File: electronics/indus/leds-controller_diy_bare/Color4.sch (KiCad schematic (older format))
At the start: 19 parts, among them Q5 Q_NPN_BCE, U3 TPS92513

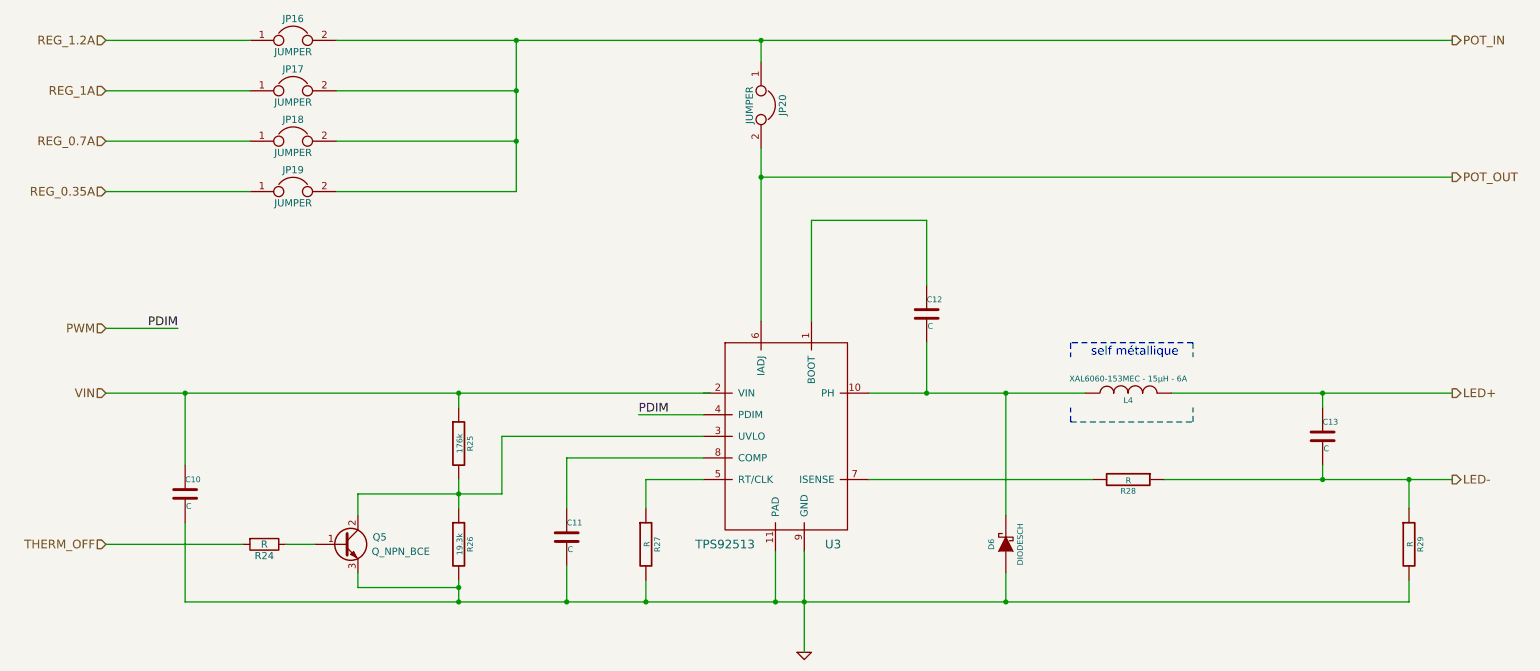
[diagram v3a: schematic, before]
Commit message: Added missing Capa & Resistor values
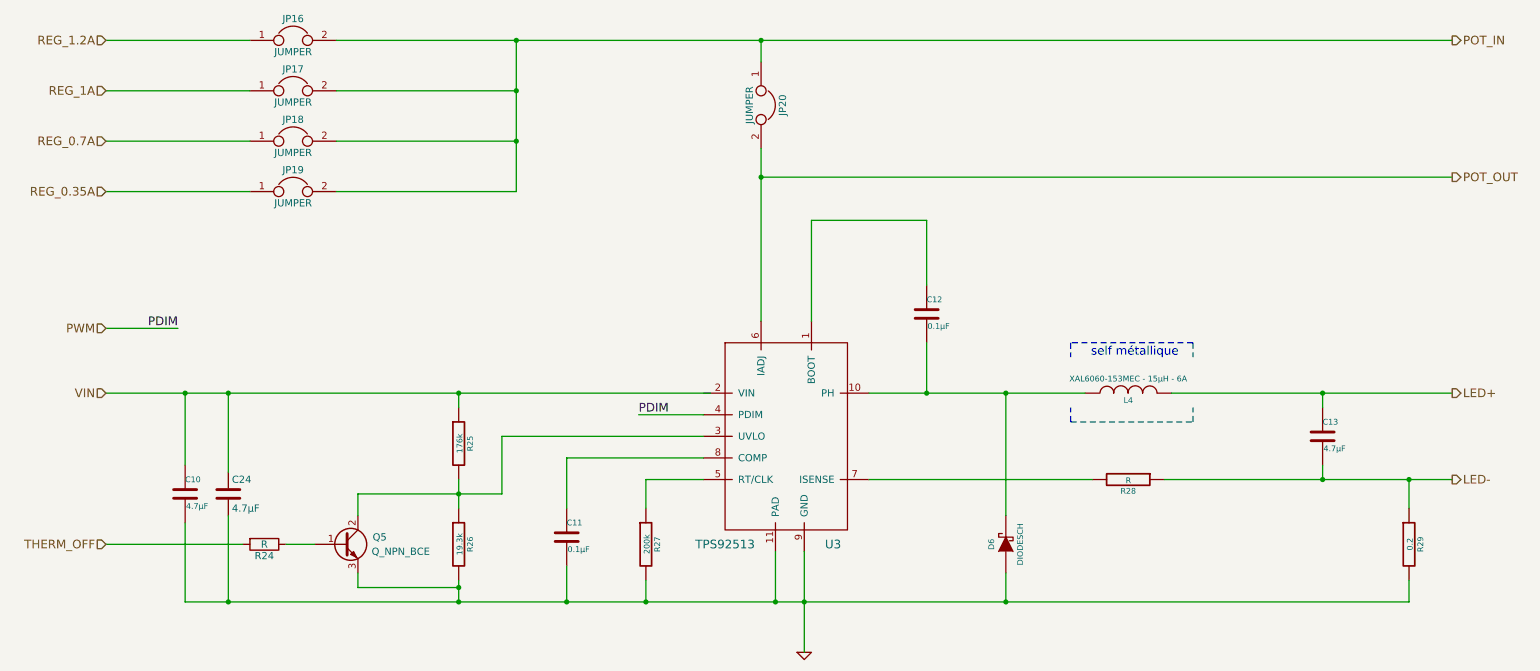
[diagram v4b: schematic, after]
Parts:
- added C24: 4.7µF, symbol C
- C10, C13: value C -> 4.7µF
- C11, C12: value C -> 0.1µF
- R27: value R -> 200k
- R29: value R -> 0.2
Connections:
- net GND: now also C24.2
- net VIN: now also C24.1
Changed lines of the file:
@@
 P 1800 4700
 F 0 "C10" H 1800 4800 40  0000 L CNN
-F 1 "C" H 1806 4615 40  0000 L CNN
+F 1 "4.7µF" H 1806 4615 40  0000 L CNN
 F 2 "" H 1838 4550 30  0000 C CNN
 F 3 "" H 1800 4700 60  0000 C CNN
@@
 P 4450 5000
 F 0 "C11" H 4450 5100 40  0000 L CNN
-F 1 "C" H 4456 4915 40  0000 L CNN
+F 1 "0.1µF" H 4456 4915 40  0000 L CNN
 F 2 "" H 4488 4850 30  0000 C CNN
 F 3 "" H 4450 5000 60  0000 C CNN
@@
 P 5000 5050
 F 0 "R27" V 5080 5050 40  0000 C CNN
-F 1 "R" V 5007 5051 40  0000 C CNN
+F 1 "200k" V 5007 5051 40  0000 C CNN
 F 2 "" V 4930 5050 30  0000 C CNN
 F 3 "" H 5000 5050 30  0000 C CNN
@@
 P 6950 3450
 F 0 "C12" H 6950 3550 40  0000 L CNN
-F 1 "C" H 6956 3365 40  0000 L CNN
+F 1 "0.1µF" H 6956 3365 40  0000 L CNN
 F 2 "" H 6988 3300 30  0000 C CNN
 F 3 "" H 6950 3450 60  0000 C CNN
@@
 P 9700 4300
 F 0 "C13" H 9700 4400 40  0000 L CNN
-F 1 "C" H 9706 4215 40  0000 L CNN
+F 1 "4.7µF" H 9706 4215 40  0000 L CNN
 F 2 "" H 9738 4150 30  0000 C CNN
 F 3 "" H 9700 4300 60  0000 C CNN
@@
 P 10300 5050
 F 0 "R29" V 10380 5050 40  0000 C CNN
-F 1 "R" V 10307 5051 40  0000 C CNN
+F 1 "0.2" V 10307 5051 40  0000 C CNN
 F 2 "" V 10230 5050 30  0000 C CNN
 F 3 "" H 10300 5050 30  0000 C CNN
@@
 POT_OUT
 Wire Wire Line
-	1250 4000 1800 4000
-Wire Wire Line
-	1800 4000 3700 4000
-Wire Wire Line
-	3700 4000 3700 4000
-Wire Wire Line
-	3700 4000 5450 4000
-Wire Wire Line
-	1800 5450 3700 5450
-Wire Wire Line
-	3700 5450 4450 5450
-Wire Wire Line
-	4450 5450 5000 5450
-Wire Wire Line
-	5000 5450 5900 5450
-Wire Wire Line
-	5900 5450 6100 5450
-Wire Wire Line
-	6100 5450 7500 5450
-Wire Wire Line
-	7500 5450 10300 5450
-Wire Wire Line
-	6100 5100 6100 5450
-Wire Wire Line
-	6100 5450 6100 5800
+	1250 4000 5450 4000
+Wire Wire Line
+	1800 5450 10300 5450
+Wire Wire Line
+	6100 5100 6100 5800
 Wire Wire Line
 	5900 5100 5900 5450
@@
 Connection ~ 6100 5450
 Wire Wire Line
-	3700 4600 3700 4700
-Wire Wire Line
-	3700 4700 3700 4800
+	3700 4600 3700 4800
 Wire Wire Line
 	4000 4700 4000 4300
@@
 	8800 3650 8800 3750
 Wire Wire Line
-	6550 4000 6950 4000
-Wire Wire Line
-	6950 4000 7500 4000
-Wire Wire Line
-	7500 4000 8050 4000
+	6550 4000 8050 4000
 Wire Wire Line
 	6150 3500 6150 2800
@@
 Connection ~ 6950 4000
 Wire Wire Line
-	8650 4000 9700 4000
-Wire Wire Line
-	9700 4000 10600 4000
+	8650 4000 10600 4000
 Wire Wire Line
 	9700 4100 9700 4000
@@
 	6550 4600 8100 4600
 Wire Wire Line
-	8600 4600 9700 4600
-Wire Wire Line
-	9700 4600 10300 4600
-Wire Wire Line
-	10300 4600 10600 4600
+	8600 4600 10600 4600
 Wire Wire Line
 	10300 4800 10300 4600
@@
 	1250 2600 2250 2600
 Wire Wire Line
-	2850 1550 4100 1550
-Wire Wire Line
-	4100 1550 5800 1550
-Wire Wire Line
-	5800 1550 10600 1550
+	2850 1550 10600 1550
 Wire Wire Line
 	2850 1900 4100 1900
 Wire Wire Line
-	4100 1550 4100 1900
-Wire Wire Line
-	4100 1900 4100 2250
-Wire Wire Line
-	4100 2250 4100 2600
+	4100 1550 4100 2600
 Connection ~ 4100 1550
 Wire Wire Line
@@
 Connection ~ 5800 2500
 Wire Wire Line
-	5800 2300 5800 2500
-Wire Wire Line
-	5800 2500 5800 3500
+	5800 2300 5800 3500
 Wire Wire Line
 	5800 1700 5800 1550
@@
 	1800 4900 1800 5450
 Wire Wire Line
-	3700 5300 3700 5350
-Wire Wire Line
-	3700 5350 3700 5450
+	3700 5300 3700 5450
 Wire Wire Line
 	3700 4100 3700 4000
@@
 	3000 4850 3000 4700
 Wire Wire Line
-	3000 4700 3700 4700
-Wire Wire Line
-	3700 4700 4000 4700
+	3000 4700 4000 4700
 Wire Wire Line
 	3000 5250 3000 5350
@@
 Wire Wire Line
 	2200 5050 1250 5050
+$Comp
+L C C24
+U 1 1 576AC01B
+P 2100 4700
+F 0 "C24" H 2125 4800 50  0000 L CNN
+F 1 "4.7µF" H 2125 4600 50  0000 L CNN
+F 2 "" H 2138 4550 50  0000 C CNN
+F 3 "" H 2100 4700 50  0000 C CNN
+	1    2100 4700
+	1    0    0    -1
+$EndComp
+Wire Wire Line
+	2100 4550 2100 4000
+Connection ~ 2100 4000
+Wire Wire Line
+	2100 4850 2100 5450
+Connection ~ 2100 5450
 $EndSCHEMATC

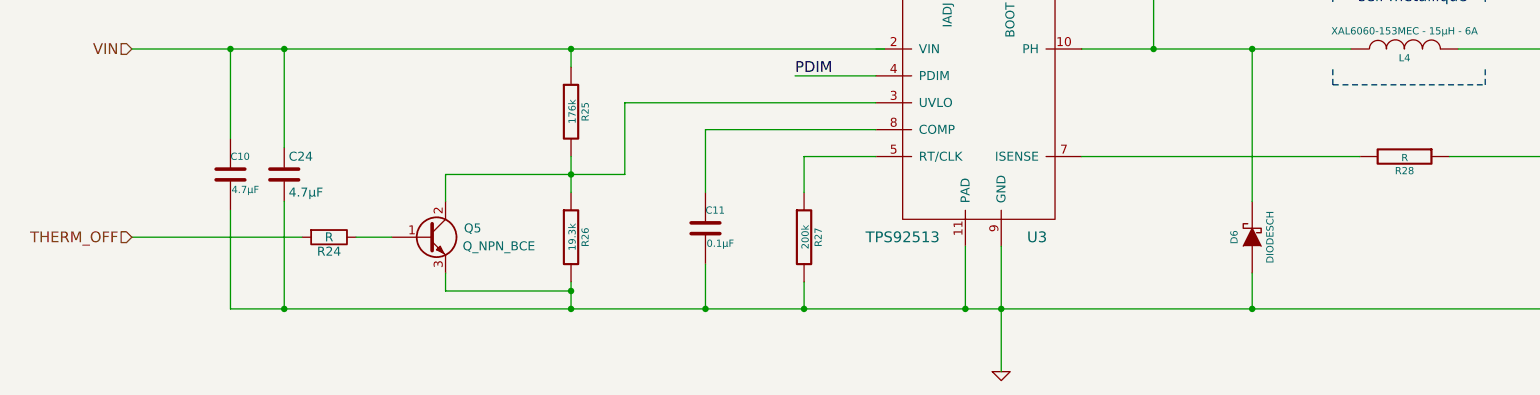
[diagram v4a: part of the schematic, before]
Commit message: footprint with libraries
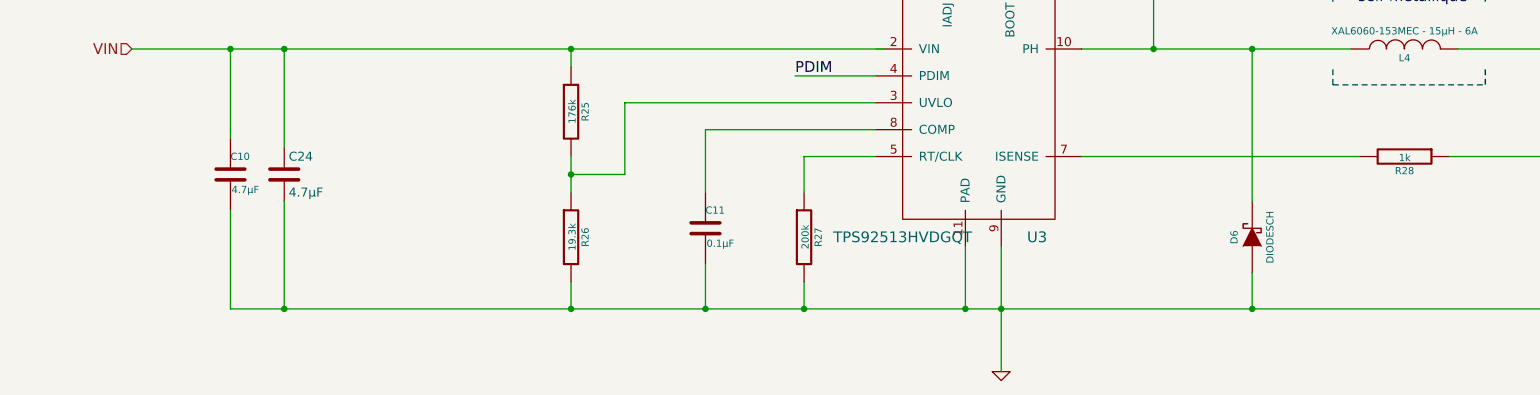
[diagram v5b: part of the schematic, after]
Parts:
- removed Q5: Q_NPN_BCE, symbol Q_NPN_BCE
- removed R24: R, symbol R
- C10, C13, C24: footprint (none) -> Capacitors_SMD:C_1206
- C11, C12: footprint (none) -> Capacitors_SMD:C_0805
- D6: footprint (none) -> Diodes_SMD:SOD-123
- R25, R26, R27: footprint (none) -> Resistors_SMD:R_0805
- R28: value R -> 1k; footprint (none) -> Resistors_SMD:R_0805
- R29: footprint (none) -> Resistors_SMD:R_1206
- U3: value TPS92513 -> TPS92513HVDGQT; footprint (none) -> risebox:BUCK_TPS92513_PowerPAD
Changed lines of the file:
@@
 P 5950 4100
 F 0 "U3" H 6300 3150 60  0000 C CNN
-F 1 "TPS92513" H 5550 3150 60  0000 C CNN
-F 2 "" H 6100 4200 60  0000 C CNN
+F 1 "TPS92513HVDGQT" H 5550 3150 60  0000 C CNN
+F 2 "risebox:BUCK_TPS92513_PowerPAD" H 6100 4200 60  0001 C CNN
 F 3 "" H 6100 4200 60  0000 C CNN
 	1    5950 4100
@@
 F 0 "C10" H 1800 4800 40  0000 L CNN
 F 1 "4.7µF" H 1806 4615 40  0000 L CNN
-F 2 "" H 1838 4550 30  0000 C CNN
+F 2 "Capacitors_SMD:C_1206" H 1838 4550 30  0001 C CNN
 F 3 "" H 1800 4700 60  0000 C CNN
 	1    1800 4700
@@
 $EndComp
 $Comp
-L GND-RESCUE-leds-controller #PWR14
+L GND-RESCUE-leds-controller #PWR015
 U 1 1 5767300B
 P 6100 5800
-F 0 "#PWR14" H 6100 5800 30  0001 C CNN
+F 0 "#PWR015" H 6100 5800 30  0001 C CNN
 F 1 "GND" H 6100 5730 30  0001 C CNN
 F 2 "" H 6100 5800 60  0000 C CNN
@@
 F 0 "R25" V 3780 4350 40  0000 C CNN
 F 1 "176k" V 3707 4351 40  0000 C CNN
-F 2 "" V 3630 4350 30  0000 C CNN
+F 2 "Resistors_SMD:R_0805" V 3630 4350 30  0001 C CNN
 F 3 "" H 3700 4350 30  0000 C CNN
 	1    3700 4350
@@
 F 0 "R26" V 3780 5050 40  0000 C CNN
 F 1 "19.3k" V 3707 5051 40  0000 C CNN
-F 2 "" V 3630 5050 30  0000 C CNN
+F 2 "Resistors_SMD:R_0805" V 3630 5050 30  0001 C CNN
 F 3 "" H 3700 5050 30  0000 C CNN
 	1    3700 5050
@@
 F 0 "C11" H 4450 5100 40  0000 L CNN
 F 1 "0.1µF" H 4456 4915 40  0000 L CNN
-F 2 "" H 4488 4850 30  0000 C CNN
+F 2 "Capacitors_SMD:C_0805" H 4488 4850 30  0001 C CNN
 F 3 "" H 4450 5000 60  0000 C CNN
 	1    4450 5000
@@
 F 0 "R27" V 5080 5050 40  0000 C CNN
 F 1 "200k" V 5007 5051 40  0000 C CNN
-F 2 "" V 4930 5050 30  0000 C CNN
+F 2 "Resistors_SMD:R_0805" V 4930 5050 30  0001 C CNN
 F 3 "" H 5000 5050 30  0000 C CNN
 	1    5000 5050
@@
 F 0 "C12" H 6950 3550 40  0000 L CNN
 F 1 "0.1µF" H 6956 3365 40  0000 L CNN
-F 2 "" H 6988 3300 30  0000 C CNN
+F 2 "Capacitors_SMD:C_0805" H 6988 3300 30  0001 C CNN
 F 3 "" H 6950 3450 60  0000 C CNN
 	1    6950 3450
@@
 F 0 "C13" H 9700 4400 40  0000 L CNN
 F 1 "4.7µF" H 9706 4215 40  0000 L CNN
-F 2 "" H 9738 4150 30  0000 C CNN
+F 2 "Capacitors_SMD:C_1206" H 9738 4150 30  0001 C CNN
 F 3 "" H 9700 4300 60  0000 C CNN
 	1    9700 4300
@@
 P 8350 4600
 F 0 "R28" V 8430 4600 40  0000 C CNN
-F 1 "R" V 8357 4601 40  0000 C CNN
-F 2 "" V 8280 4600 30  0000 C CNN
+F 1 "1k" V 8357 4601 40  0000 C CNN
+F 2 "Resistors_SMD:R_0805" V 8280 4600 30  0001 C CNN
 F 3 "" H 8350 4600 30  0000 C CNN
 	1    8350 4600
@@
 F 0 "R29" V 10380 5050 40  0000 C CNN
 F 1 "0.2" V 10307 5051 40  0000 C CNN
-F 2 "" V 10230 5050 30  0000 C CNN
+F 2 "Resistors_SMD:R_1206" V 10230 5050 30  0001 C CNN
 F 3 "" H 10300 5050 30  0000 C CNN
 	1    10300 5050
@@
 F 0 "D6" H 7500 5150 40  0000 C CNN
 F 1 "DIODESCH" H 7500 4950 40  0000 C CNN
-F 2 "" H 7500 5050 60  0000 C CNN
+F 2 "Diodes_SMD:SOD-123" H 7500 5050 60  0001 C CNN
 F 3 "" H 7500 5050 60  0000 C CNN
 	1    7500 5050
@@
 F 0 "JP16" H 2550 1700 50  0000 C CNN
 F 1 "JUMPER" H 2550 1470 50  0000 C CNN
-F 2 "" H 2550 1550 50  0000 C CNN
+F 2 "" H 2550 1550 50  0001 C CNN
 F 3 "" H 2550 1550 50  0000 C CNN
 	1    2550 1550
@@
 F 0 "JP17" H 2550 2050 50  0000 C CNN
 F 1 "JUMPER" H 2550 1820 50  0000 C CNN
-F 2 "" H 2550 1900 50  0000 C CNN
+F 2 "" H 2550 1900 50  0001 C CNN
 F 3 "" H 2550 1900 50  0000 C CNN
 	1    2550 1900
@@
 F 0 "JP18" H 2550 2400 50  0000 C CNN
 F 1 "JUMPER" H 2550 2170 50  0000 C CNN
-F 2 "" H 2550 2250 50  0000 C CNN
+F 2 "" H 2550 2250 50  0001 C CNN
 F 3 "" H 2550 2250 50  0000 C CNN
 	1    2550 2250
@@
 F 0 "JP19" H 2550 2750 50  0000 C CNN
 F 1 "JUMPER" H 2550 2520 50  0000 C CNN
-F 2 "" H 2550 2600 50  0000 C CNN
+F 2 "" H 2550 2600 50  0001 C CNN
 F 3 "" H 2550 2600 50  0000 C CNN
 	1    2550 2600
@@
 F 0 "JP20" H 5800 2150 50  0000 C CNN
 F 1 "JUMPER" H 5800 1920 50  0000 C CNN
-F 2 "" H 5800 2000 50  0000 C CNN
+F 2 "" H 5800 2000 50  0001 C CNN
 F 3 "" H 5800 2000 50  0000 C CNN
 	1    5800 2000
@@
 Connection ~ 3700 5450
 Wire Wire Line
-	3000 4850 3000 4700
-Wire Wire Line
-	3000 4700 4000 4700
-Wire Wire Line
-	3000 5250 3000 5350
-Wire Wire Line
-	3000 5350 3700 5350
-Connection ~ 3700 5350
-$Comp
-L Q_NPN_BCE Q5
-U 1 1 576730E6
-P 2900 5050
-F 0 "Q5" H 3200 5100 50  0000 R CNN
-F 1 "Q_NPN_BCE" H 3500 5000 50  0000 R CNN
-F 2 "" H 3100 5150 50  0000 C CNN
-F 3 "" H 2900 5050 50  0000 C CNN
-	1    2900 5050
-	1    0    0    -1
-$EndComp
-Text HLabel 1250 5050 0    60   Input ~ 0
-THERM_OFF
-$Comp
-L R R24
-U 1 1 576730EE
-P 2350 5050
-F 0 "R24" V 2430 5050 50  0000 C CNN
-F 1 "R" V 2350 5050 50  0000 C CNN
-F 2 "" V 2280 5050 50  0000 C CNN
-F 3 "" H 2350 5050 50  0000 C CNN
-	1    2350 5050
-	0    1    1    0
-$EndComp
-Wire Wire Line
-	2500 5050 2700 5050
-Wire Wire Line
-	2200 5050 1250 5050
+	3700 4700 4000 4700
 $Comp
 L C C24
@@
 F 0 "C24" H 2125 4800 50  0000 L CNN
 F 1 "4.7µF" H 2125 4600 50  0000 L CNN
-F 2 "" H 2138 4550 50  0000 C CNN
+F 2 "Capacitors_SMD:C_1206" H 2138 4550 50  0001 C CNN
 F 3 "" H 2100 4700 50  0000 C CNN
 	1    2100 4700

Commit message: fix some errors
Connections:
- net VIN: now also U3.2 (VIN)
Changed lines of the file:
@@
 Text HLabel 10600 4600 2    60   Output ~ 0
 LED-
-Text HLabel 1250 4000 0    60   Input ~ 0
+Text HLabel 1300 4000 0    60   Input ~ 0
 VIN
 $Comp
@@
 POT_OUT
 Wire Wire Line
-	1250 4000 5450 4000
+	1300 4000 5400 4000
 Wire Wire Line
 	1800 5450 10300 5450
@@
 	5800 1700 5800 1550
 Wire Wire Line
-	1800 4500 1800 4000
-Connection ~ 1800 4000
+	1800 4500 1850 4000
+Connection ~ 1850 4000
 Wire Wire Line
 	1800 4900 1800 5450
@@
 	3700 5300 3700 5450
 Wire Wire Line
-	3700 4100 3700 4000
-Connection ~ 3700 4000
+	3700 4100 3650 4000
+Connection ~ 3650 4000
 Connection ~ 3700 5450
 Wire Wire Line

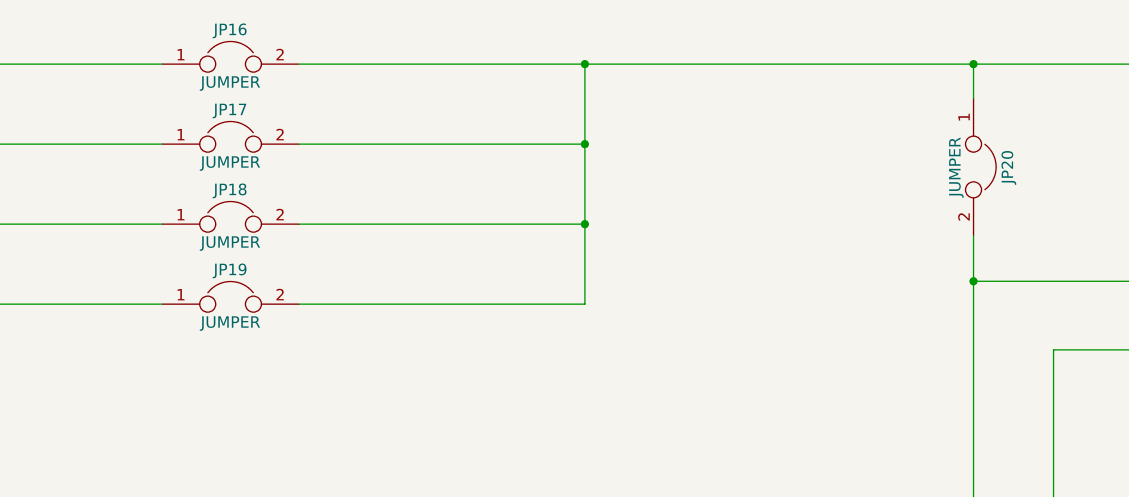
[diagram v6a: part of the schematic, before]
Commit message: add pinhead footprint
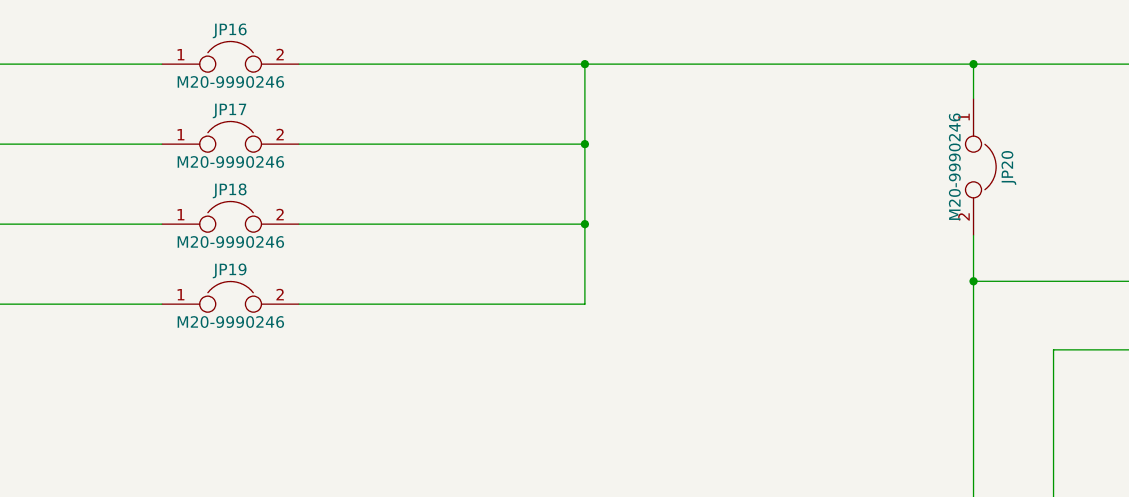
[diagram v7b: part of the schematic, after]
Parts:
- JP16, JP17, JP18, JP19, JP20: value JUMPER -> M20-9990246; footprint (none) -> Connect:PINHEAD1-2
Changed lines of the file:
@@
 P 2550 1550
 F 0 "JP16" H 2550 1700 50  0000 C CNN
-F 1 "JUMPER" H 2550 1470 50  0000 C CNN
-F 2 "" H 2550 1550 50  0001 C CNN
+F 1 "M20-9990246" H 2550 1470 50  0000 C CNN
+F 2 "Connect:PINHEAD1-2" H 2550 1550 50  0001 C CNN
 F 3 "" H 2550 1550 50  0000 C CNN
 	1    2550 1550
@@
 P 2550 1900
 F 0 "JP17" H 2550 2050 50  0000 C CNN
-F 1 "JUMPER" H 2550 1820 50  0000 C CNN
-F 2 "" H 2550 1900 50  0001 C CNN
+F 1 "M20-9990246" H 2550 1820 50  0000 C CNN
+F 2 "Connect:PINHEAD1-2" H 2550 1900 50  0001 C CNN
 F 3 "" H 2550 1900 50  0000 C CNN
 	1    2550 1900
@@
 P 2550 2250
 F 0 "JP18" H 2550 2400 50  0000 C CNN
-F 1 "JUMPER" H 2550 2170 50  0000 C CNN
-F 2 "" H 2550 2250 50  0001 C CNN
+F 1 "M20-9990246" H 2550 2170 50  0000 C CNN
+F 2 "Connect:PINHEAD1-2" H 2550 2250 50  0001 C CNN
 F 3 "" H 2550 2250 50  0000 C CNN
 	1    2550 2250
@@
 P 2550 2600
 F 0 "JP19" H 2550 2750 50  0000 C CNN
-F 1 "JUMPER" H 2550 2520 50  0000 C CNN
-F 2 "" H 2550 2600 50  0001 C CNN
+F 1 "M20-9990246" H 2550 2520 50  0000 C CNN
+F 2 "Connect:PINHEAD1-2" H 2550 2600 50  0001 C CNN
 F 3 "" H 2550 2600 50  0000 C CNN
 	1    2550 2600
@@
 P 5800 2000
 F 0 "JP20" H 5800 2150 50  0000 C CNN
-F 1 "JUMPER" H 5800 1920 50  0000 C CNN
-F 2 "" H 5800 2000 50  0001 C CNN
+F 1 "M20-9990246" H 5800 1920 50  0000 C CNN
+F 2 "Connect:PINHEAD1-2" H 5800 2000 50  0001 C CNN
 F 3 "" H 5800 2000 50  0000 C CNN
 	1    5800 2000
